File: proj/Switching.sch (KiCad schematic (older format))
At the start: 13 parts, among them Q7 MMBT3906, Q8 2N7002, Q9 2N7002, U10 MASWSS0162, U9 MASWSS0162

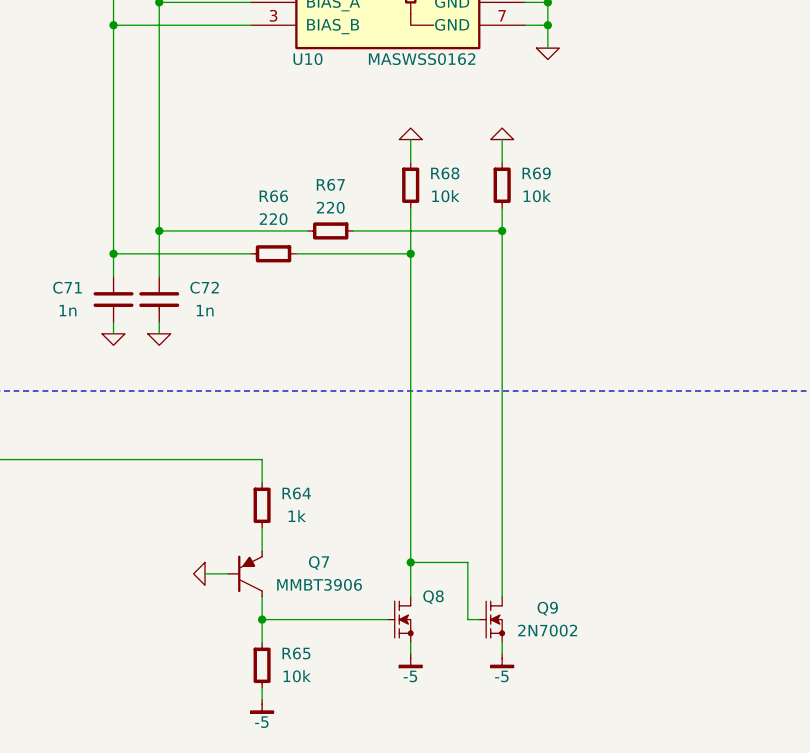
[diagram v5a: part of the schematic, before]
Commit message: Clean up resistor BOM
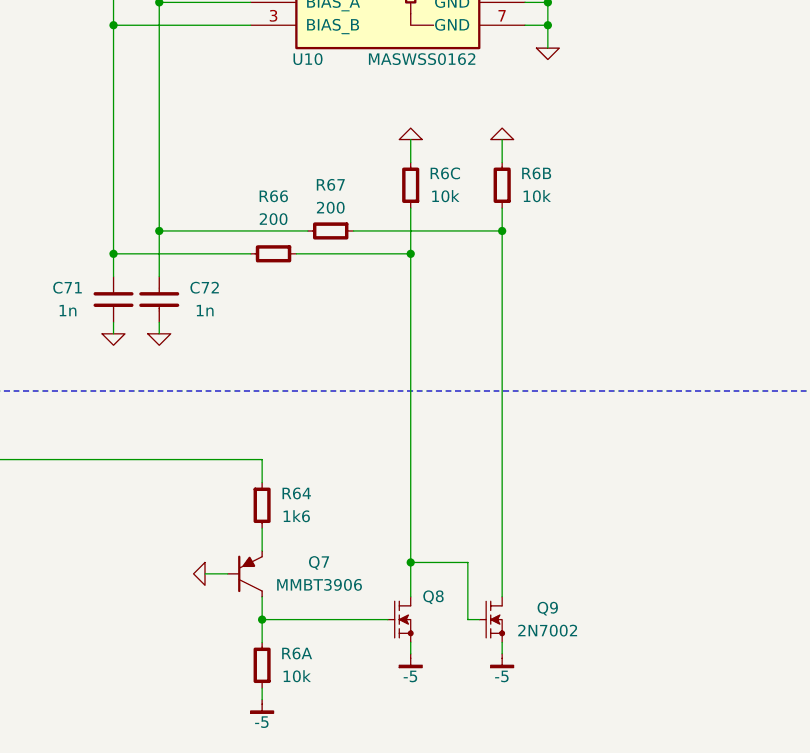
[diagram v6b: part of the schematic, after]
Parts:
- removed R65, R68, R69: 10k, IPC7351-Nominal:RESC1005X40, symbol R-0402
- added R6: 10k, IPC7351-Nominal:RESCAXE80P160X320X70-8, symbol RESPACK-4X0603-CONV
- R64: value 1k -> 1k6; BOM RES SMD 1k 5% [0402] -> RES SMD 1.6k 5% [0402]
- R66, R67: value 220 -> 200; BOM RES SMD 220 5% [0402] -> RES SMD 200 5% [0402]
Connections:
- net -5: now also R6.1
- net GND: now also R6.6, R6.7
- net at Q8.3, Q9.1, R66.1: now also R6.3
- net at Q9.3, R67.1: now also R6.2
- net at Q7.3, Q8.1: now also R6.8
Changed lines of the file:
@@
 $Descr USLegal 14000 8500
 encoding utf-8
-Sheet 9 13
+Sheet 8 13
 Title "Input Switching"
 Date "2015-02-28"
@@
 P 6100 4500
 F 0 "R66" V 5850 4500 50  0000 C CNN
-F 1 "220" V 5950 4500 50  0000 C CNN
+F 1 "200" V 5950 4500 50  0000 C CNN
 F 2 "IPC7351-Nominal:RESC1005X40" H 6100 4500 50  0001 C CNN
 F 3 "" H 6100 4550 60  0000 C CNN
 F 4 "Value" H 6100 4500 60  0001 C CNN "Manuf"
-F 5 "RES SMD 220 5% [0402]" H 6850 5050 60  0001 C CNN "BOM"
+F 5 "RES SMD 200 5% [0402]" H 6850 5050 60  0001 C CNN "BOM"
 	1    6100 4500
 	0    1    1    0
@@
 P 6350 4400
 F 0 "R67" V 6150 4400 50  0000 C CNN
-F 1 "220" V 6250 4400 50  0000 C CNN
+F 1 "200" V 6250 4400 50  0000 C CNN
 F 2 "IPC7351-Nominal:RESC1005X40" H 6350 4400 50  0001 C CNN
 F 3 "" H 6350 4450 60  0000 C CNN
 F 4 "Value" H 6350 4400 60  0001 C CNN "Manuf"
-F 5 "RES SMD 220 5% [0402]" H 7100 4950 60  0001 C CNN "BOM"
+F 5 "RES SMD 200 5% [0402]" H 7100 4950 60  0001 C CNN "BOM"
 	1    6350 4400
 	0    1    1    0
 $EndComp
 $Comp
-L R-0402 R68
-U 1 1 54F35056
-P 6700 4200
-F 0 "R68" H 6850 4250 50  0000 C CNN
-F 1 "10k" H 6850 4150 50  0000 C CNN
-F 2 "IPC7351-Nominal:RESC1005X40" H 6700 4200 50  0001 C CNN
-F 3 "" H 6700 4250 60  0000 C CNN
-F 4 "Value" H 6700 4200 60  0001 C CNN "Manuf"
-F 5 "RES SMD 10k 5% [0402]" H 7450 4750 60  0001 C CNN "BOM"
-	1    6700 4200
-	1    0    0    -1
-$EndComp
-$Comp
-L GND #PWR0172
+L GND #PWR0170
 U 1 1 54F35197
 P 6700 4000
-F 0 "#PWR0172" H 6700 4000 30  0001 C CNN
+F 0 "#PWR0170" H 6700 4000 30  0001 C CNN
 F 1 "GND" H 6700 3930 30  0001 C CNN
 F 2 "" H 6700 4000 60  0000 C CNN
@@
 $EndComp
 $Comp
-L R-0402 R69
-U 1 1 54F351E5
-P 7100 4200
-F 0 "R69" H 7250 4250 50  0000 C CNN
-F 1 "10k" H 7250 4150 50  0000 C CNN
-F 2 "IPC7351-Nominal:RESC1005X40" H 7100 4200 50  0001 C CNN
-F 3 "" H 7100 4250 60  0000 C CNN
-F 4 "Value" H 7100 4200 60  0001 C CNN "Manuf"
-F 5 "RES SMD 10k 5% [0402]" H 7850 4750 60  0001 C CNN "BOM"
-	1    7100 4200
-	1    0    0    -1
-$EndComp
-$Comp
-L GND #PWR0173
+L GND #PWR0171
 U 1 1 54F3526C
 P 7100 4000
-F 0 "#PWR0173" H 7100 4000 30  0001 C CNN
+F 0 "#PWR0171" H 7100 4000 30  0001 C CNN
 F 1 "GND" H 7100 3930 30  0001 C CNN
 F 2 "" H 7100 4000 60  0000 C CNN
@@
 $EndComp
 $Comp
-L GND #PWR0174
+L GND #PWR0172
 U 1 1 54F3552B
 P 5400 4850
-F 0 "#PWR0174" H 5400 4850 30  0001 C CNN
+F 0 "#PWR0172" H 5400 4850 30  0001 C CNN
 F 1 "GND" H 5400 4780 30  0001 C CNN
 F 2 "" H 5400 4850 60  0000 C CNN
@@
 $EndComp
 $Comp
-L GND #PWR0175
+L GND #PWR0173
 U 1 1 54F3557E
 P 5600 4850
-F 0 "#PWR0175" H 5600 4850 30  0001 C CNN
+F 0 "#PWR0173" H 5600 4850 30  0001 C CNN
 F 1 "GND" H 5600 4780 30  0001 C CNN
 F 2 "" H 5600 4850 60  0000 C CNN
@@
 Connection ~ 6700 5850
 $Comp
-L -5 #PWR0176
+L -5 #PWR0174
 U 1 1 54F35B7E
 P 6700 6250
-F 0 "#PWR0176" H 6700 6200 30  0001 C CNN
+F 0 "#PWR0174" H 6700 6200 30  0001 C CNN
 F 1 "-5" H 6700 6150 50  0000 C CNN
 F 2 "" H 6700 6250 60  0000 C CNN
@@
 	6700 6250 6700 6200
 $Comp
-L -5 #PWR0177
+L -5 #PWR0175
 U 1 1 54F35BE5
 P 7100 6250
-F 0 "#PWR0177" H 7100 6200 30  0001 C CNN
+F 0 "#PWR0175" H 7100 6200 30  0001 C CNN
 F 1 "-5" H 7100 6150 50  0000 C CNN
 F 2 "" H 7100 6250 60  0000 C CNN
@@
 Wire Wire Line
 	7100 6250 7100 6200
-$Comp
-L R-0402 R65
-U 1 1 54F35C3E
-P 6050 6300
-F 0 "R65" H 6200 6350 50  0000 C CNN
-F 1 "10k" H 6200 6250 50  0000 C CNN
-F 2 "IPC7351-Nominal:RESC1005X40" H 6050 6300 50  0001 C CNN
-F 3 "" H 6050 6350 60  0000 C CNN
-F 4 "Value" H 6050 6300 60  0001 C CNN "Manuf"
-F 5 "RES SMD 10k 5% [0402]" H 6800 6850 60  0001 C CNN "BOM"
-	1    6050 6300
-	1    0    0    -1
-$EndComp
 Wire Wire Line
 	6050 6000 6050 6200
@@
 	6050 6100 6600 6100
 $Comp
-L -5 #PWR0178
+L -5 #PWR0176
 U 1 1 54F35DDE
 P 6050 6450
-F 0 "#PWR0178" H 6050 6400 30  0001 C CNN
+F 0 "#PWR0176" H 6050 6400 30  0001 C CNN
 F 1 "-5" H 6050 6350 50  0000 C CNN
 F 2 "" H 6050 6450 60  0000 C CNN
@@
 P 6050 5600
 F 0 "R64" H 6200 5650 50  0000 C CNN
-F 1 "1k" H 6200 5550 50  0000 C CNN
+F 1 "1k6" H 6200 5550 50  0000 C CNN
 F 2 "IPC7351-Nominal:RESC1005X40" H 6050 5600 50  0001 C CNN
 F 3 "" H 6050 5650 60  0000 C CNN
 F 4 "Value" H 6050 5600 60  0001 C CNN "Manuf"
-F 5 "RES SMD 1k 5% [0402]" H 6800 6150 60  0001 C CNN "BOM"
+F 5 "RES SMD 1.6k 5% [0402]" H 6800 6150 60  0001 C CNN "BOM"
 	1    6050 5600
 	1    0    0    -1
@@
 $EndComp
 $Comp
-L GND #PWR0179
+L GND #PWR0177
 U 1 1 54F35FD4
 P 5800 5900
-F 0 "#PWR0179" H 5800 5900 30  0001 C CNN
+F 0 "#PWR0177" H 5800 5900 30  0001 C CNN
 F 1 "GND" H 5800 5830 30  0001 C CNN
 F 2 "" H 5800 5900 60  0000 C CNN
@@
 CTRL
 $Comp
-L GND #PWR0180
+L GND #PWR0178
 U 1 1 54F36542
 P 7300 3600
-F 0 "#PWR0180" H 7300 3600 30  0001 C CNN
+F 0 "#PWR0178" H 7300 3600 30  0001 C CNN
 F 1 "GND" H 7300 3530 30  0001 C CNN
 F 2 "" H 7300 3600 60  0000 C CNN
@@
 	1    0    0    -1
 $EndComp
+$Comp
+L RESPACK-4X0603-CONV R6
+U 1 1 54FD633A
+P 6050 6300
+AR Path="/54F1FB16/54F2F9AC/54FD633A" Ref="R6"  Part="1"
+AR Path="/54F1FAFD/54FD633A" Ref="R6"  Part="4"
+F 0 "R6" H 5900 6250 50  0000 C CNN
+F 1 "10k" H 5900 6350 50  0000 C CNN
+F 2 "IPC7351-Nominal:RESCAXE80P160X320X70-8" H 6050 6300 50  0001 C CNN
+F 3 "" H 6050 6350 60  0000 C CNN
+F 4 "YC164-JR-0710KL" H 6050 6300 60  0001 C CNN "PN"
+F 5 "Yageo" H 6050 6300 60  0001 C CNN "Manuf"
+F 6 "DIST DIGIKEY YC164J-10KCT-ND" H 6050 6300 60  0001 C CNN "BOM"
+	1    6050 6300
+	-1   0    0    1
+$EndComp
+$Comp
+L RESPACK-4X0603-CONV R6
+U 3 1 54FD63A4
+P 6700 4200
+F 0 "R6" H 6550 4150 50  0000 C CNN
+F 1 "10k" H 6550 4250 50  0000 C CNN
+F 2 "IPC7351-Nominal:RESCAXE80P160X320X70-8" H 6700 4200 50  0001 C CNN
+F 3 "" H 6700 4250 60  0000 C CNN
+F 4 "YC164-JR-0710KL" H 6700 4200 60  0001 C CNN "PN"
+F 5 "Yageo" H 6700 4200 60  0001 C CNN "Manuf"
+F 6 "DIST DIGIKEY YC164J-10KCT-ND" H 6700 4200 60  0001 C CNN "BOM"
+	3    6700 4200
+	-1   0    0    1
+$EndComp
+$Comp
+L RESPACK-4X0603-CONV R6
+U 2 1 54FD63F6
+P 7100 4200
+F 0 "R6" H 6950 4150 50  0000 C CNN
+F 1 "10k" H 6950 4250 50  0000 C CNN
+F 2 "IPC7351-Nominal:RESCAXE80P160X320X70-8" H 7100 4200 50  0001 C CNN
+F 3 "" H 7100 4250 60  0000 C CNN
+F 4 "YC164-JR-0710KL" H 7100 4200 60  0001 C CNN "PN"
+F 5 "Yageo" H 7100 4200 60  0001 C CNN "Manuf"
+F 6 "DIST DIGIKEY YC164J-10KCT-ND" H 7100 4200 60  0001 C CNN "BOM"
+	2    7100 4200
+	-1   0    0    1
+$EndComp
 $EndSCHEMATC

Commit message: Swap 0402 to 0603, add USB inrush protection
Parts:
- removed C71, C72: 1n, IPC7351-Nominal:CAPC1005X55, symbol C-0402
- removed R64: 1k6, IPC7351-Nominal:RESC1005X40, symbol R-0402
- removed R66, R67: 200, IPC7351-Nominal:RESC1005X40, symbol R-0402
- added C71, C72: 1n, IPC7351-Nominal:CAPC1608X55, symbol C-0603
- added R64: 1k6, IPC7351-Nominal:RESC1608X50, symbol R-0603
- added R66, R67: 200, IPC7351-Nominal:RESC1608X50, symbol R-0603
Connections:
- net CTRL: now also R64.1
- net GND: now also C71.2, C72.2
- net at U10.3 (BIAS_B), U9.2 (BIAS_A): now also C71.1, R66.2
- net at U10.2 (BIAS_A), U9.3 (BIAS_B): now also C72.1, R67.2
- net at Q8.3, Q9.1, R6.3: now also R66.1
- net at Q9.3, R6.2: now also R67.1
- net at Q7.2: now also R64.2
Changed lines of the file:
@@
 Layout: These stubs must be /very/ short!
 $Comp
-L C-0402 C71
-U 1 1 54F34AF4
-P 5400 4700
-F 0 "C71" H 5600 4750 50  0000 C CNN
-F 1 "1n" H 5600 4650 50  0000 C CNN
-F 2 "IPC7351-Nominal:CAPC1005X55" H 5400 4700 50  0001 C CNN
-F 3 "" H 5390 4675 60  0000 C CNN
-F 4 "Value" H 5400 4700 60  0001 C CNN "Manuf"
-F 5 "CAP MLCC 1nF C0G 10V 5% [0402]" H 6200 5250 60  0001 C CNN "BOM"
-	1    5400 4700
-	-1   0    0    -1
-$EndComp
-$Comp
-L C-0402 C72
-U 1 1 54F34B15
-P 5600 4700
-F 0 "C72" H 5800 4750 50  0000 C CNN
-F 1 "1n" H 5800 4650 50  0000 C CNN
-F 2 "IPC7351-Nominal:CAPC1005X55" H 5600 4700 50  0001 C CNN
-F 3 "" H 5590 4675 60  0000 C CNN
-F 4 "Value" H 5600 4700 60  0001 C CNN "Manuf"
-F 5 "CAP MLCC 1nF C0G 10V 5% [0402]" H 6400 5250 60  0001 C CNN "BOM"
-	1    5600 4700
-	1    0    0    -1
-$EndComp
-$Comp
-L R-0402 R66
-U 1 1 54F34BE3
-P 6100 4500
-F 0 "R66" V 5850 4500 50  0000 C CNN
-F 1 "200" V 5950 4500 50  0000 C CNN
-F 2 "IPC7351-Nominal:RESC1005X40" H 6100 4500 50  0001 C CNN
-F 3 "" H 6100 4550 60  0000 C CNN
-F 4 "Value" H 6100 4500 60  0001 C CNN "Manuf"
-F 5 "RES SMD 200 5% [0402]" H 6850 5050 60  0001 C CNN "BOM"
-	1    6100 4500
-	0    1    1    0
-$EndComp
-$Comp
-L R-0402 R67
-U 1 1 54F34D1E
-P 6350 4400
-F 0 "R67" V 6150 4400 50  0000 C CNN
-F 1 "200" V 6250 4400 50  0000 C CNN
-F 2 "IPC7351-Nominal:RESC1005X40" H 6350 4400 50  0001 C CNN
-F 3 "" H 6350 4450 60  0000 C CNN
-F 4 "Value" H 6350 4400 60  0001 C CNN "Manuf"
-F 5 "RES SMD 200 5% [0402]" H 7100 4950 60  0001 C CNN "BOM"
-	1    6350 4400
-	0    1    1    0
-$EndComp
-$Comp
-L GND #PWR0170
+L GND #PWR0163
 U 1 1 54F35197
 P 6700 4000
-F 0 "#PWR0170" H 6700 4000 30  0001 C CNN
+F 0 "#PWR0163" H 6700 4000 30  0001 C CNN
 F 1 "GND" H 6700 3930 30  0001 C CNN
 F 2 "" H 6700 4000 60  0000 C CNN
@@
 $EndComp
 $Comp
-L GND #PWR0171
+L GND #PWR0164
 U 1 1 54F3526C
 P 7100 4000
-F 0 "#PWR0171" H 7100 4000 30  0001 C CNN
+F 0 "#PWR0164" H 7100 4000 30  0001 C CNN
 F 1 "GND" H 7100 3930 30  0001 C CNN
 F 2 "" H 7100 4000 60  0000 C CNN
@@
 $EndComp
 $Comp
-L GND #PWR0172
+L GND #PWR0165
 U 1 1 54F3552B
 P 5400 4850
-F 0 "#PWR0172" H 5400 4850 30  0001 C CNN
+F 0 "#PWR0165" H 5400 4850 30  0001 C CNN
 F 1 "GND" H 5400 4780 30  0001 C CNN
 F 2 "" H 5400 4850 60  0000 C CNN
@@
 $EndComp
 $Comp
-L GND #PWR0173
+L GND #PWR0166
 U 1 1 54F3557E
 P 5600 4850
-F 0 "#PWR0173" H 5600 4850 30  0001 C CNN
+F 0 "#PWR0166" H 5600 4850 30  0001 C CNN
 F 1 "GND" H 5600 4780 30  0001 C CNN
 F 2 "" H 5600 4850 60  0000 C CNN
@@
 Connection ~ 6700 5850
 $Comp
-L -5 #PWR0174
+L -5 #PWR0167
 U 1 1 54F35B7E
 P 6700 6250
-F 0 "#PWR0174" H 6700 6200 30  0001 C CNN
+F 0 "#PWR0167" H 6700 6200 30  0001 C CNN
 F 1 "-5" H 6700 6150 50  0000 C CNN
 F 2 "" H 6700 6250 60  0000 C CNN
@@
 	6700 6250 6700 6200
 $Comp
-L -5 #PWR0175
+L -5 #PWR0168
 U 1 1 54F35BE5
 P 7100 6250
-F 0 "#PWR0175" H 7100 6200 30  0001 C CNN
+F 0 "#PWR0168" H 7100 6200 30  0001 C CNN
 F 1 "-5" H 7100 6150 50  0000 C CNN
 F 2 "" H 7100 6250 60  0000 C CNN
@@
 	6050 6100 6600 6100
 $Comp
-L -5 #PWR0176
+L -5 #PWR0169
 U 1 1 54F35DDE
 P 6050 6450
-F 0 "#PWR0176" H 6050 6400 30  0001 C CNN
+F 0 "#PWR0169" H 6050 6400 30  0001 C CNN
 F 1 "-5" H 6050 6350 50  0000 C CNN
 F 2 "" H 6050 6450 60  0000 C CNN
@@
 Wire Wire Line
 	6050 6450 6050 6400
-$Comp
-L R-0402 R64
-U 1 1 54F35E96
-P 6050 5600
-F 0 "R64" H 6200 5650 50  0000 C CNN
-F 1 "1k6" H 6200 5550 50  0000 C CNN
-F 2 "IPC7351-Nominal:RESC1005X40" H 6050 5600 50  0001 C CNN
-F 3 "" H 6050 5650 60  0000 C CNN
-F 4 "Value" H 6050 5600 60  0001 C CNN "Manuf"
-F 5 "RES SMD 1.6k 5% [0402]" H 6800 6150 60  0001 C CNN "BOM"
-	1    6050 5600
-	1    0    0    -1
-$EndComp
 $Comp
 L MMBT3906 Q7
@@
 $EndComp
 $Comp
-L GND #PWR0177
+L GND #PWR0170
 U 1 1 54F35FD4
 P 5800 5900
-F 0 "#PWR0177" H 5800 5900 30  0001 C CNN
+F 0 "#PWR0170" H 5800 5900 30  0001 C CNN
 F 1 "GND" H 5800 5830 30  0001 C CNN
 F 2 "" H 5800 5900 60  0000 C CNN
@@
 CTRL
 $Comp
-L GND #PWR0178
+L GND #PWR0171
 U 1 1 54F36542
 P 7300 3600
-F 0 "#PWR0178" H 7300 3600 30  0001 C CNN
+F 0 "#PWR0171" H 7300 3600 30  0001 C CNN
 F 1 "GND" H 7300 3530 30  0001 C CNN
 F 2 "" H 7300 3600 60  0000 C CNN
@@
 	-1   0    0    1
 $EndComp
+$Comp
+L R-0603 R64
+U 1 1 5504344E
+P 6050 5600
+F 0 "R64" H 6200 5650 50  0000 C CNN
+F 1 "1k6" H 6200 5550 50  0000 C CNN
+F 2 "IPC7351-Nominal:RESC1608X50" H 6050 5600 50  0001 C CNN
+F 3 "" H 6050 5650 60  0000 C CNN
+F 4 "Value" H 6050 5600 60  0001 C CNN "Manuf"
+F 5 "RES SMD 1.6k 1% [0603]" H 6800 6150 60  0001 C CNN "BOM"
+	1    6050 5600
+	1    0    0    -1
+$EndComp
+$Comp
+L R-0603 R67
+U 1 1 55044AA5
+P 6350 4400
+F 0 "R67" V 6150 4400 50  0000 C CNN
+F 1 "200" V 6250 4400 50  0000 C CNN
+F 2 "IPC7351-Nominal:RESC1608X50" H 6350 4400 50  0001 C CNN
+F 3 "" H 6350 4450 60  0000 C CNN
+F 4 "Value" H 6350 4400 60  0001 C CNN "Manuf"
+F 5 "RES SMD 200 1% [0603]" H 7100 4950 60  0001 C CNN "BOM"
+	1    6350 4400
+	0    1    1    0
+$EndComp
+$Comp
+L R-0603 R66
+U 1 1 55044C5F
+P 6100 4500
+F 0 "R66" V 5850 4500 50  0000 C CNN
+F 1 "200" V 5950 4500 50  0000 C CNN
+F 2 "IPC7351-Nominal:RESC1608X50" H 6100 4500 50  0001 C CNN
+F 3 "" H 6100 4550 60  0000 C CNN
+F 4 "Value" H 6100 4500 60  0001 C CNN "Manuf"
+F 5 "RES SMD 200 1% [0603]" H 6850 5050 60  0001 C CNN "BOM"
+	1    6100 4500
+	0    1    1    0
+$EndComp
+$Comp
+L C-0603 C71
+U 1 1 55046FF6
+P 5400 4700
+F 0 "C71" H 5600 4750 50  0000 C CNN
+F 1 "1n" H 5600 4650 50  0000 C CNN
+F 2 "IPC7351-Nominal:CAPC1608X55" H 5400 4700 50  0001 C CNN
+F 3 "" H 5390 4675 60  0000 C CNN
+F 4 "Value" H 5400 4700 60  0001 C CNN "Manuf"
+F 5 "CAP MLCC 1n C0G 50V 10% [0603]" H 6200 5250 60  0001 C CNN "BOM"
+	1    5400 4700
+	-1   0    0    -1
+$EndComp
+$Comp
+L C-0603 C72
+U 1 1 55047017
+P 5600 4700
+F 0 "C72" H 5800 4750 50  0000 C CNN
+F 1 "1n" H 5800 4650 50  0000 C CNN
+F 2 "IPC7351-Nominal:CAPC1608X55" H 5600 4700 50  0001 C CNN
+F 3 "" H 5590 4675 60  0000 C CNN
+F 4 "Value" H 5600 4700 60  0001 C CNN "Manuf"
+F 5 "CAP MLCC 1n C0G 50V 10% [0603]" H 6400 5250 60  0001 C CNN "BOM"
+	1    5600 4700
+	1    0    0    -1
+$EndComp
 $EndSCHEMATC
